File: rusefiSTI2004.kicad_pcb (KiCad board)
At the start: 2 copper layers, 138.6 x 113.6 mm, 137 parts, among them J1 TE_1-1376430-0, J2 USB C 2.0 16P, J3 Molex_39281143, M1 Module-mega-mcu144-0.7, M10 Module-lin-0.1, M11 Module-dinput4-0.1, M12 Module-dinput4-0.1, M13 Module-knock-0.2, M14 Module-power_12and5V-0.3, M2 Module-motor-driver-0.1, M3 Module-wbo-0.5, M5 Module-vr-discrete-0.5, M8 Module-power_12and5V-0.3, M9 Module-motor-driver-0.1, P1 WBO_UN, P10 OUT_SPARE_LS2, P11 CHARGE_A22, P12 FP_STATUS, P13 DLC6_D29, P14 SPARE_IGN6, P15 SPARE_IGN7, P16 SPARE_IGN8, P17 I2C_1_SCL, P18 I2C_1_SDA, P19 +5VA, P2 WBO_VM, P20 +3.3V, P21 +12V_RAW, P22 GND, P23 BOOT0, P24 SWDIO, P25 SWCLK, P26 NRST, P27 SPARE_PWM3, P28 SPARE_RES2, P29 AUX_IN1, P3 WBO_IP, P30 AUX_IN2, P31 AUX_IN3, P32 PG_5VP_APS, P4 WBO_RTRIM, P5 WBO_HEATER, P6 CAN_H, P7 CAN_L, P8 K_LINE, P9 OUT_SPARE_LS1, Q1 NCV8401BDTRKG, Q10 NCV8401BDTRKG, Q11 NCV8401BDTRKG, Q12 NCV8401BDTRKG, Q13 NCV8401BDTRKG, Q14 NCV8401BDTRKG, Q15 NCV8401BDTRKG, Q16 NCV8401BDTRKG, Q17 NCV8401BDTRKG, Q18 NCV8401BDTRKG, Q19 NCV8401BDTRKG, Q2 NCV8401BDTRKG, Q20 NCV8401BDTRKG, Q3 NCV8401BDTRKG, Q4 NCV8401BDTRKG, Q5 NCV8401BDTRKG, Q6 NCV8401BDTRKG, Q7 NCV8401BDTRKG, Q8 NCV8401BDTRKG, Q9 NCV8401BDTRKG, U1 USBLC6-2SC6

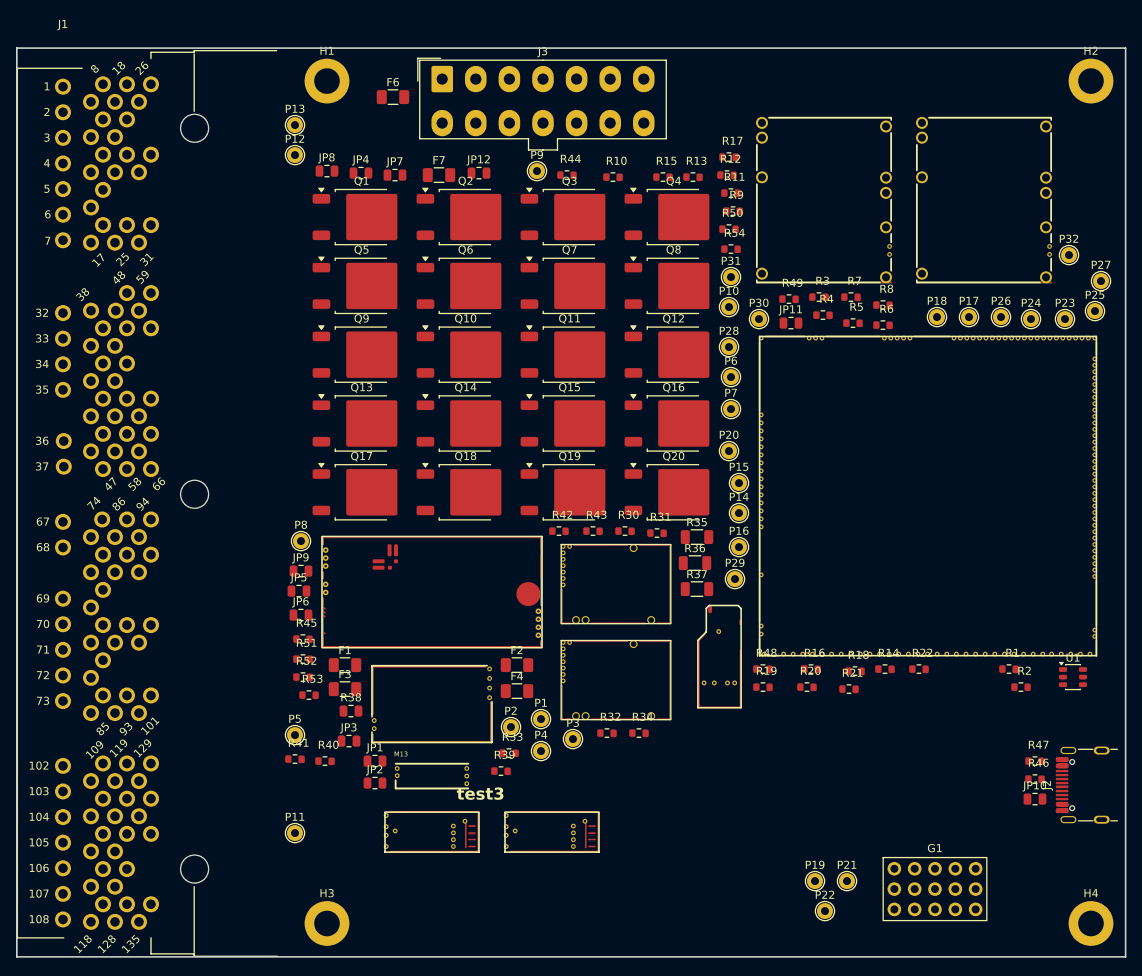
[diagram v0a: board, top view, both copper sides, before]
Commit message: PCB: 4 layers with In1 GND plane, all parts on top spaced for routing, JLC-size silk references
- Hellen modules carry In1/In2 copper and the Hellen build defaults to 4 layers.
- Board Setup floors lowered to JLC capability (0.2 mm hole, 0.15 mm hole clearance); scoped DRC
  exceptions for J2, M13 and J1 GND spokes. DRC 0 errors, parity 0.
- Stray rev-a 'test3' board text removed.

Co-Authored-By: Claude Opus 5.5 <noreply@anthropic.com>
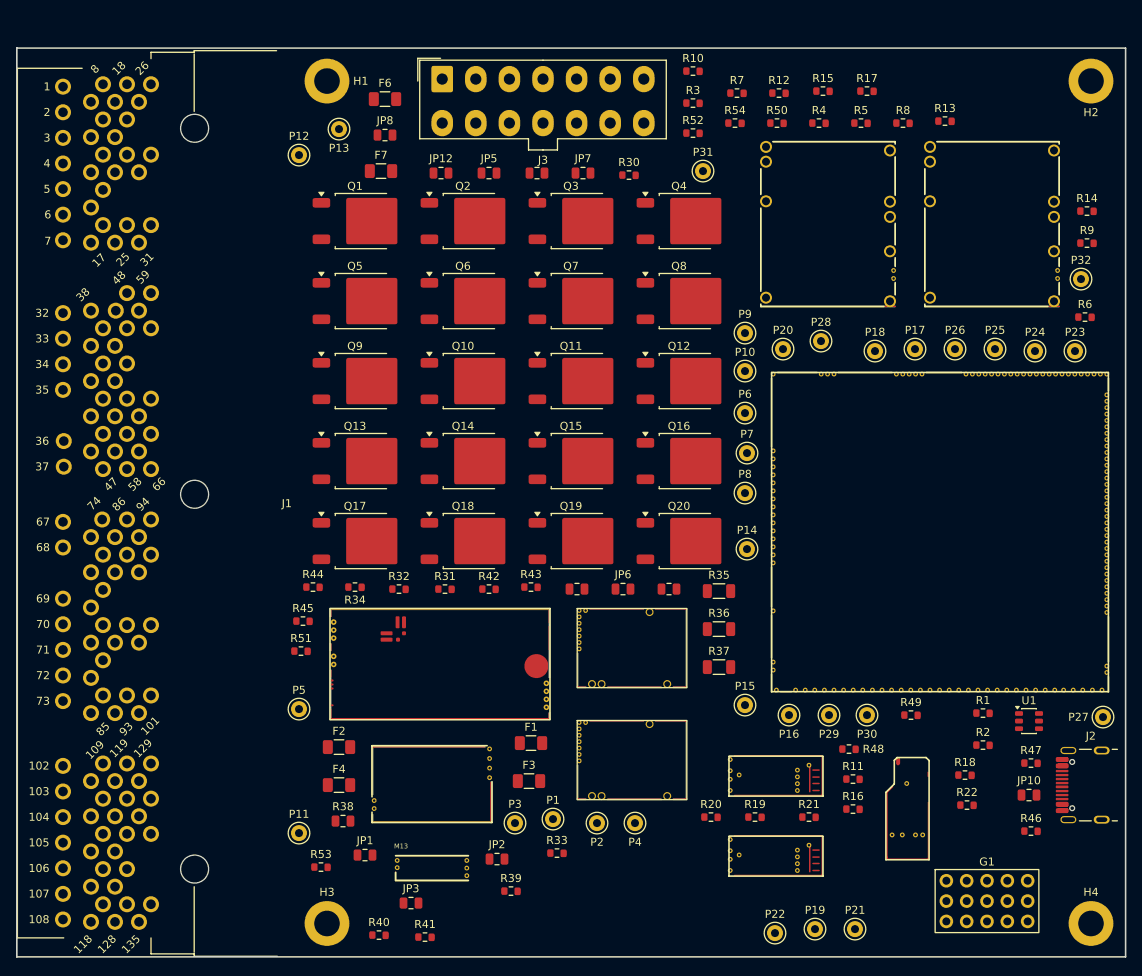
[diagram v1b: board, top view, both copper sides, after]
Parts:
- moved R52 83.7 mm to (169.8, 46.5)
- moved R11 74.8 mm to (189.8, 127.2)
- moved R14 62.6 mm to (219.0, 56.2)
- moved R44 60.5 mm to (122.2, 103.2)
- moved JP5 57.4 mm to (144.2, 51.5)
- moved P8 55.8 mm to (176.2, 91.5)
- moved P27 54.5 mm to (221.0, 119.5)
- moved R49 54.2 mm to (197.0, 119.2)
- moved P30 51.3 mm to (191.5, 119.2)
- moved R30 44.5 mm to (161.8, 51.8)
- moved R9 44.4 mm to (219.0, 60.2)
- moved M11 43.6 mm to (174.2, 129.5)
- moved JP6 40.4 mm to (161.0, 103.5)
- moved R34 39.9 mm to (127.5, 103.2)
- moved JP11 36.6 mm to (166.8, 103.5)
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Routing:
- added copper zone on In1.Cu, net GND
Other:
- copper layers 2 -> 4
- board text removed: "test3"

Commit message: Planes: In1 GND, In2 +12V_RAW, top/bottom GND pours with stitching, DPAK drain heat spreaders with thermal vias
DRC 0 errors, parity 0; unconnected 482 -> 326 (ground and +12V_RAW pads now join their planes).

Co-Authored-By: Claude Opus 5.5 <noreply@anthropic.com>
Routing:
- net OUT_WG: vias 0 -> 6
- net OUT_VVT_RH-: vias 0 -> 6
- net OUT_VVT_LH-: vias 0 -> 6
- net OUT_TACH: vias 0 -> 6
- net OUT_SPARE_LS2: vias 0 -> 6
- net OUT_SPARE_LS1: vias 0 -> 6
- net OUT_PURGE_CONTROL: vias 0 -> 6
- net OUT_O2_HEATER_REAR: vias 0 -> 6
- net OUT_MIL: vias 0 -> 6
- net OUT_MAIN_RELAY: vias 0 -> 6
- net OUT_INJ4: vias 0 -> 6
- net OUT_INJ3: vias 0 -> 6
- net OUT_INJ2: vias 0 -> 6
- net OUT_INJ1: vias 0 -> 6
- net OUT_FAN_RELAY_2: vias 0 -> 6
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- added copper zone on In2.Cu, net +12V_RAW
- added copper zone on B.Cu, net GND
- added copper zone on F.Cu, net GND
- added copper zone on B.Cu, net OUT_AC_RELAY
- added copper zone on F.Cu, net OUT_AC_RELAY
- added copper zone on B.Cu, net OUT_CRUISE_MAIN_LIGHT
- added copper zone on F.Cu, net OUT_CRUISE_MAIN_LIGHT
- added copper zone on B.Cu, net OUT_CRUISE_SET_LIGHT
- added copper zone on F.Cu, net OUT_CRUISE_SET_LIGHT
- added copper zone on B.Cu, net OUT_ELECTRONIC_THROTTE_RELAY
- added copper zone on F.Cu, net OUT_ELECTRONIC_THROTTE_RELAY
- added copper zone on B.Cu, net OUT_FAN_RELAY_1
- added copper zone on F.Cu, net OUT_FAN_RELAY_1
- added copper zone on B.Cu, net OUT_FAN_RELAY_2
- added copper zone on F.Cu, net OUT_FAN_RELAY_2
- added copper zone on B.Cu, net OUT_INJ1
- added copper zone on F.Cu, net OUT_INJ1
- added copper zone on B.Cu, net OUT_INJ2
- added copper zone on F.Cu, net OUT_INJ2
- added copper zone on B.Cu, net OUT_INJ3
- added copper zone on F.Cu, net OUT_INJ3
- added copper zone on B.Cu, net OUT_INJ4
- added copper zone on F.Cu, net OUT_INJ4
- added copper zone on B.Cu, net OUT_MAIN_RELAY
- added copper zone on F.Cu, net OUT_MAIN_RELAY
- added copper zone on B.Cu, net OUT_MIL
- added copper zone on F.Cu, net OUT_MIL
- added copper zone on B.Cu, net OUT_O2_HEATER_REAR
- added copper zone on F.Cu, net OUT_O2_HEATER_REAR
- added copper zone on B.Cu, net OUT_PURGE_CONTROL
- added copper zone on F.Cu, net OUT_PURGE_CONTROL
- added copper zone on B.Cu, net OUT_SPARE_LS1
- added copper zone on F.Cu, net OUT_SPARE_LS1
- added copper zone on B.Cu, net OUT_SPARE_LS2
- added copper zone on F.Cu, net OUT_SPARE_LS2
- added copper zone on B.Cu, net OUT_TACH
- added copper zone on F.Cu, net OUT_TACH
- added copper zone on B.Cu, net OUT_VVT_LH-
- added copper zone on F.Cu, net OUT_VVT_LH-
- added copper zone on B.Cu, net OUT_VVT_RH-
- added copper zone on F.Cu, net OUT_VVT_RH-
- added copper zone on B.Cu, net OUT_WG
- added copper zone on F.Cu, net OUT_WG

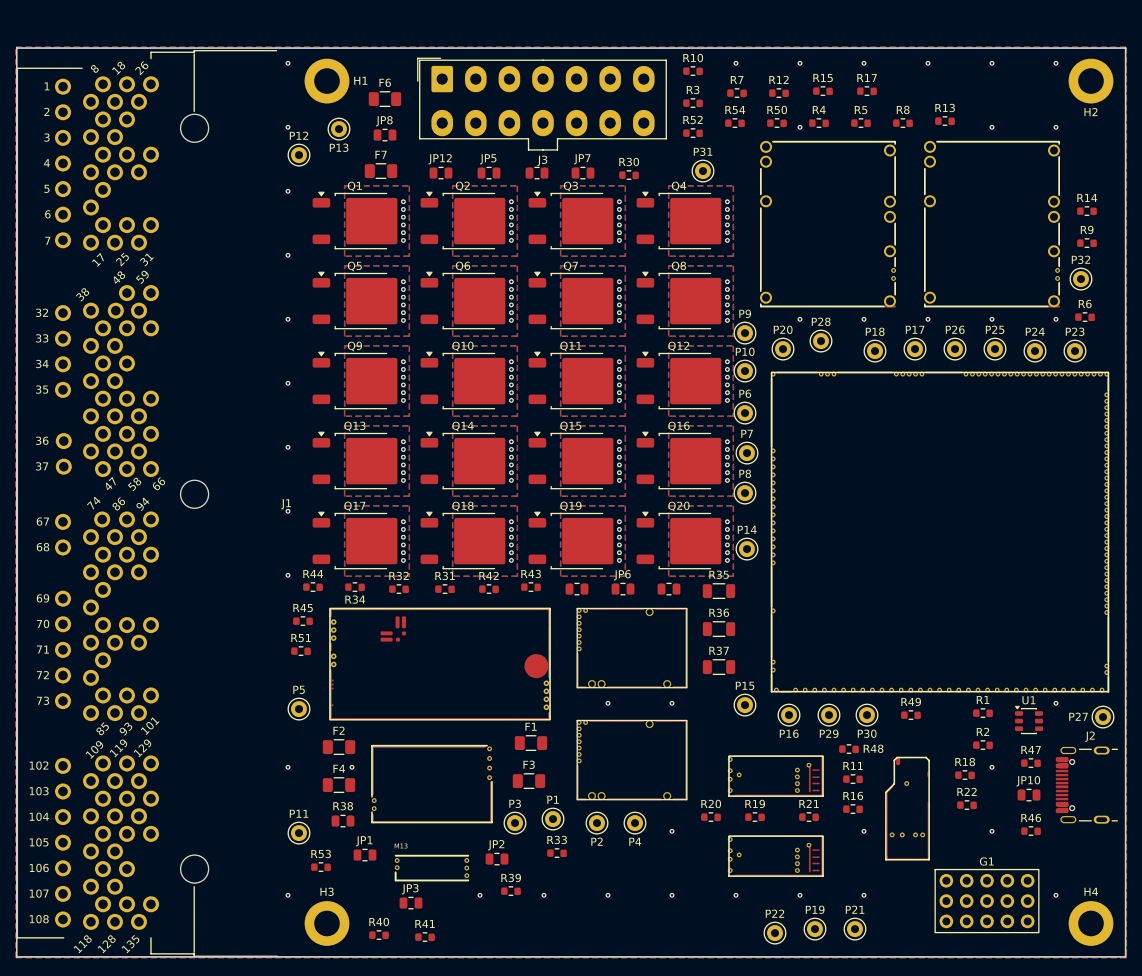
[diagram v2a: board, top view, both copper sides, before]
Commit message: Low-side drivers sized per load: 8 DPAK (NCV8401B), 4 SOT-223 (ZXMS6006DGQ), 8 SOT-23F (ZXMS6004FF)
INJ and LS2 stay DPAK; LS3 and LS1/LS4 use new sub-sheets with the smaller parts. Purge and the rear
O2 heater swapped groups (LS2/LS3), spares moved to LS3, MIL/tach to LS4; every output keeps its
J1 and MCU pin (checked on the netlist). PCB bank re-placed, planes rebuilt: DRC 0 errors, parity 0.

Co-Authored-By: Claude Opus 5.5 <noreply@anthropic.com>
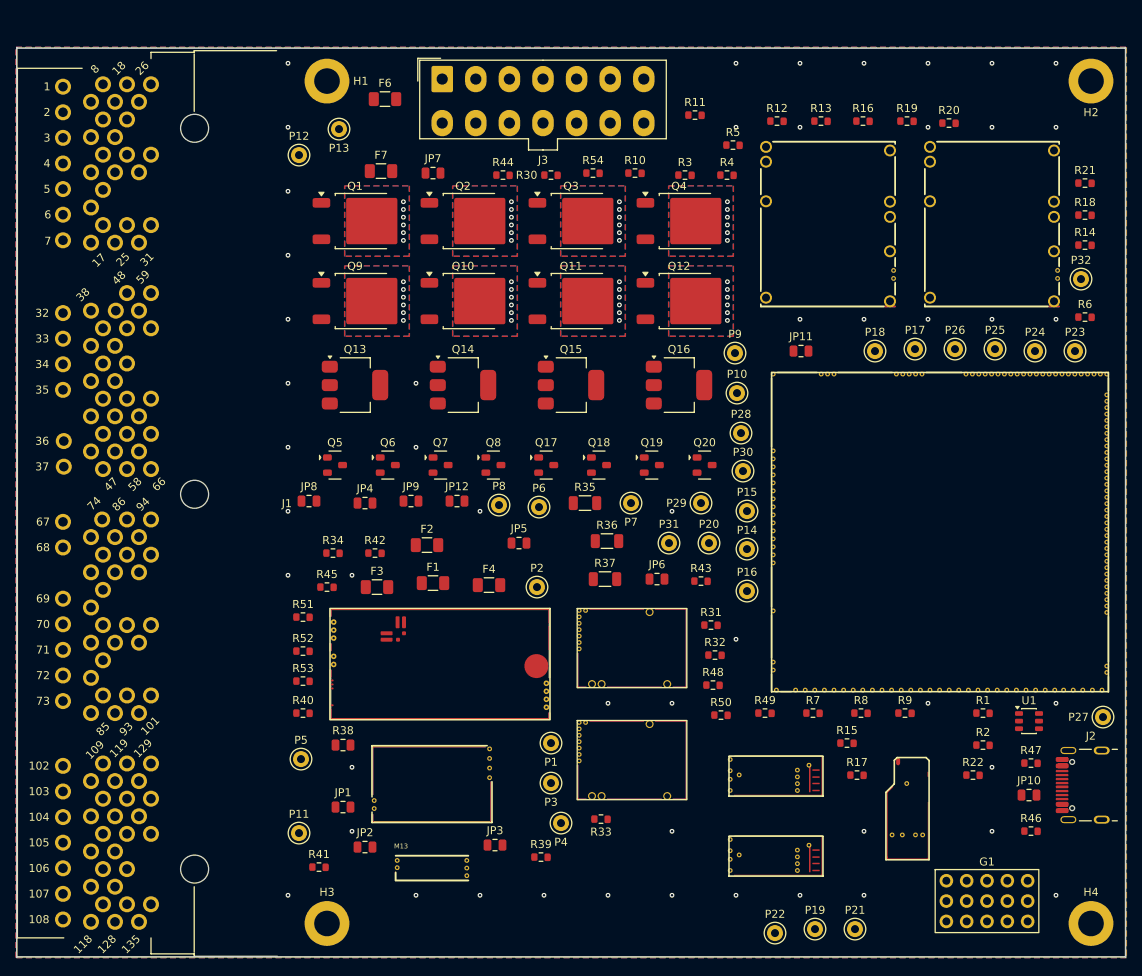
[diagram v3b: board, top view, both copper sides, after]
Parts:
- Q13, Q14, Q15, Q16: value NCV8401BDTRKG -> ZXMS6006DGQ-13; footprint EmbeddedEra_Library:TO-252-2 -> EmbeddedEra_Library:SOT-223-3_TabPin2
- Q17, Q18, Q19, Q20, Q5, Q6, Q7, Q8: value NCV8401BDTRKG -> ZXMS6004FFTA; footprint EmbeddedEra_Library:TO-252-2 -> EmbeddedEra_Library:SOT-23F_Diodes
- moved R20 91.7 mm to (201.8, 45.2)
- moved R19 89.1 mm to (196.5, 45.0)
- moved R21 86.4 mm to (218.8, 52.8)
- moved R16 86.0 mm to (191.0, 45.0)
- moved R17 85.5 mm to (190.2, 126.8)
- moved R11 85.3 mm to (170.0, 44.2)
- moved R15 81.6 mm to (189.0, 122.8)
- moved R52 81.1 mm to (121.0, 111.2)
- moved R7 78.1 mm to (184.8, 119.0)
- moved R50 74.3 mm to (173.2, 119.2)
- moved R8 73.9 mm to (190.8, 119.0)
- moved R18 71.6 mm to (218.8, 56.8)
- moved R9 63.0 mm to (196.2, 119.0)
- moved R44 56.7 mm to (146.0, 51.8)
- moved JP8 46.7 mm to (121.8, 92.5)
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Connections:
- Q12 pad 1: PURGE -> O2_HEATER_REAR
- Q12 pad 2: OUT_PURGE_CONTROL -> OUT_O2_HEATER_REAR
- Q13 pad 1: MIL -> PURGE
- Q13 pad 2: OUT_MIL -> OUT_PURGE_CONTROL
- Q14 pad 1: O2_HEATER_REAR -> AC_RELAY
- Q14 pad 2: OUT_O2_HEATER_REAR -> OUT_AC_RELAY
- Q15 pad 1: AC_RELAY -> SPARE_LS1
- Q15 pad 2: OUT_AC_RELAY -> OUT_SPARE_LS1
- Q16 pad 1: TACH -> SPARE_LS2
- Q16 pad 2: OUT_TACH -> OUT_SPARE_LS2
- Q17 pad 2: OUT_CRUISE_MAIN_LIGHT -> GND
- Q17 pad 3: GND -> OUT_CRUISE_MAIN_LIGHT
- Q18 pad 2: OUT_CRUISE_SET_LIGHT -> GND
- Q18 pad 3: GND -> OUT_CRUISE_SET_LIGHT
- Q19 pad 1: SPARE_LS1 -> MIL
- Q19 pad 2: OUT_SPARE_LS1 -> GND
- Q19 pad 3: GND -> OUT_MIL
- Q20 pad 1: SPARE_LS2 -> TACH
- Q20 pad 2: OUT_SPARE_LS2 -> GND
- Q20 pad 3: GND -> OUT_TACH
- Q5 pad 2: OUT_MAIN_RELAY -> GND
- Q5 pad 3: GND -> OUT_MAIN_RELAY
- Q6 pad 2: OUT_FAN_RELAY_1 -> GND
- Q6 pad 3: GND -> OUT_FAN_RELAY_1
- Q7 pad 2: OUT_FAN_RELAY_2 -> GND
- Q7 pad 3: GND -> OUT_FAN_RELAY_2
- Q8 pad 2: OUT_ELECTRONIC_THROTTE_RELAY -> GND
- Q8 pad 3: GND -> OUT_ELECTRONIC_THROTTE_RELAY
- R14 pad 1: PURGE -> O2_HEATER_REAR
- R15 pad 1: MIL -> PURGE
- R16 pad 1: O2_HEATER_REAR -> AC_RELAY
- R17 pad 1: AC_RELAY -> SPARE_LS1
- R18 pad 1: TACH -> SPARE_LS2
- R21 pad 1: SPARE_LS1 -> MIL
- R22 pad 1: SPARE_LS2 -> TACH
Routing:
- net OUT_TACH: vias 6 -> 0
- net OUT_SPARE_LS2: vias 6 -> 0
- net OUT_SPARE_LS1: vias 6 -> 0
- net OUT_PURGE_CONTROL: vias 6 -> 0
- net OUT_MIL: vias 6 -> 0
- net OUT_MAIN_RELAY: vias 6 -> 0
- net OUT_FAN_RELAY_2: vias 6 -> 0
- net OUT_FAN_RELAY_1: vias 6 -> 0
- net OUT_ELECTRONIC_THROTTE_RELAY: vias 6 -> 0
- net OUT_CRUISE_SET_LIGHT: vias 6 -> 0
- net OUT_CRUISE_MAIN_LIGHT: vias 6 -> 0
- net OUT_AC_RELAY: vias 6 -> 0
- net GND: vias 41 -> 51
- removed copper zone on B.Cu, net OUT_AC_RELAY
- removed copper zone on F.Cu, net OUT_AC_RELAY
- removed copper zone on B.Cu, net OUT_CRUISE_MAIN_LIGHT
- removed copper zone on F.Cu, net OUT_CRUISE_MAIN_LIGHT
- removed copper zone on B.Cu, net OUT_CRUISE_SET_LIGHT
- removed copper zone on F.Cu, net OUT_CRUISE_SET_LIGHT
- removed copper zone on B.Cu, net OUT_ELECTRONIC_THROTTE_RELAY
- removed copper zone on F.Cu, net OUT_ELECTRONIC_THROTTE_RELAY
- removed copper zone on B.Cu, net OUT_FAN_RELAY_1
- removed copper zone on F.Cu, net OUT_FAN_RELAY_1
- removed copper zone on B.Cu, net OUT_FAN_RELAY_2
- removed copper zone on F.Cu, net OUT_FAN_RELAY_2
- removed copper zone on B.Cu, net OUT_MAIN_RELAY
- removed copper zone on F.Cu, net OUT_MAIN_RELAY
- removed copper zone on B.Cu, net OUT_MIL
- removed copper zone on F.Cu, net OUT_MIL
- removed copper zone on B.Cu, net OUT_PURGE_CONTROL
- removed copper zone on F.Cu, net OUT_PURGE_CONTROL
- removed copper zone on B.Cu, net OUT_SPARE_LS1
- removed copper zone on F.Cu, net OUT_SPARE_LS1
- removed copper zone on B.Cu, net OUT_SPARE_LS2
- removed copper zone on F.Cu, net OUT_SPARE_LS2
- removed copper zone on B.Cu, net OUT_TACH
- removed copper zone on F.Cu, net OUT_TACH
